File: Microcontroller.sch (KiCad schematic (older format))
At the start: 32 parts, among them J3 USB_B, J4 SWD, J5 DEBUG, Q1 BC817, U3 STM32F401VETx, U4 USBUF02W6, Y1 8MHz

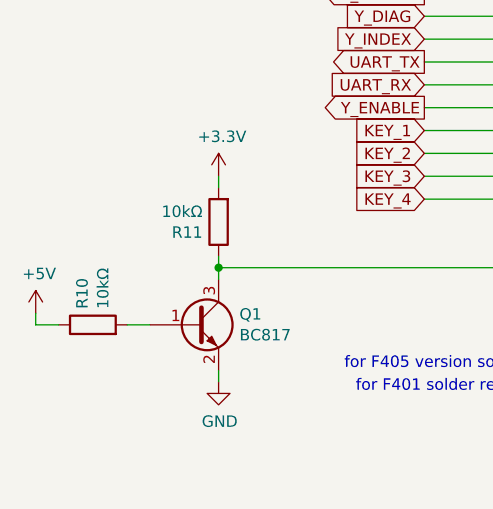
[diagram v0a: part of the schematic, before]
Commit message: Improve Emergency, Added TVS diodes
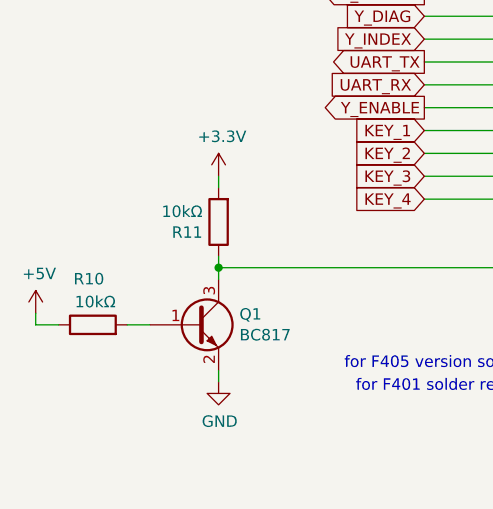
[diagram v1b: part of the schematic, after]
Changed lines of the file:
@@
 AR Path="/5E1018C2/5E3329E9" Ref="R?"  Part="1"
 AR Path="/5DFB2EC0/5E3329E9" Ref="R10"  Part="1"
-F 0 "R10" H 1120 6546 50  0000 L CNN
-F 1 "10kΩ" H 1120 6455 50  0000 L CNN
+F 0 "R10" V 1250 6450 50  0000 L CNN
+F 1 "10kΩ" V 1150 6400 50  0000 L CNN
 F 2 "Resistor_SMD:R_0603_1608Metric" V 980 6500 50  0001 C CNN
 F 3 "~" H 1050 6500 50  0001 C CNN
@@
 Connection ~ 4350 1200
 $Comp
-L power:PWR_FLAG #FLG05
+L power:PWR_FLAG #FLG01
 U 1 1 5E51609C
 P 8850 5750
-F 0 "#FLG05" H 8850 5825 50  0001 C CNN
+F 0 "#FLG01" H 8850 5825 50  0001 C CNN
 F 1 "PWR_FLAG" H 8850 5923 50  0000 C CNN
 F 2 "" H 8850 5750 50  0001 C CNN
@@
 	9900 5200 9900 5250
 $Comp
-L power:PWR_FLAG #FLG06
+L power:PWR_FLAG #FLG02
 U 1 1 5E56BFE7
 P 8950 5250
-F 0 "#FLG06" H 8950 5325 50  0001 C CNN
+F 0 "#FLG02" H 8950 5325 50  0001 C CNN
 F 1 "PWR_FLAG" H 8950 5423 50  0000 C CNN
 F 2 "" H 8950 5250 50  0001 C CNN

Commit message: Update USBUF02W6
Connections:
- net D-: now reaches J3.2 (D-), U4.4 (D3)
- net D+: now reaches J3.3 (D+), U4.6 (D4)
- net USB_DM renamed USB_D-
- net USB_DP renamed USB_D+
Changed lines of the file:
@@
 	4650 3950 5000 3950
 Text GLabel 5000 2750 2    50   BiDi ~ 0
-USB_DP
-Text GLabel 5000 2650 2    50   BiDi ~ 0
-USB_DM
+USB_D+
 Wire Wire Line
 	4650 2650 5000 2650
@@
 	8600 1400 8600 1450
 Text GLabel 9150 1800 2    50   BiDi ~ 0
-USB_DM
+USB_D-
 Text GLabel 9150 1700 2    50   BiDi ~ 0
-USB_DP
+USB_D+
 Wire Wire Line
 	8950 1700 9150 1700
@@
 Wire Wire Line
 	2750 2050 2750 2250
+Text Label 8050 1700 0    50   ~ 0
+D+
+Text Label 8050 1800 0    50   ~ 0
+D-
+Text GLabel 5000 2650 2    50   BiDi ~ 0
+USB_D-
 $EndSCHEMATC

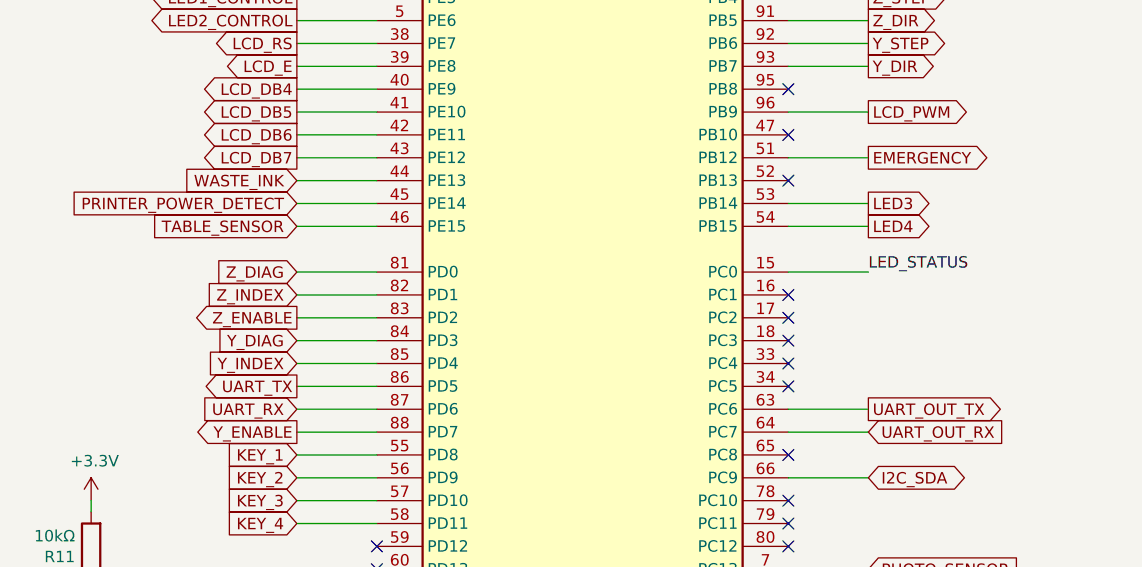
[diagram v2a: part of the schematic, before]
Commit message: Added 12V regulator, aditional input, outputs, improved inputs ESD
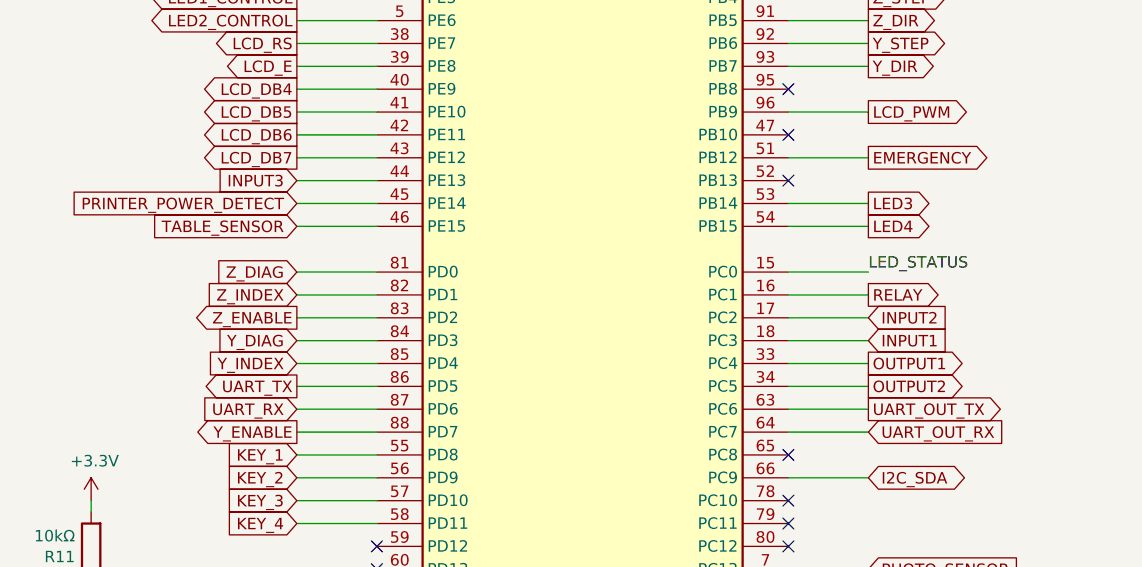
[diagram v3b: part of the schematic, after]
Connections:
- net RELAY: now reaches U3.16 (PC1)
- net INPUT2: now reaches U3.17 (PC2)
- net INPUT1: now reaches U3.18 (PC3)
- net OUTPUT1: now reaches U3.33 (PC4)
- net OUTPUT2: now reaches U3.34 (PC5)
- net WASTE_INK renamed INPUT3
- no-connect marks 28 -> 23
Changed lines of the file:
@@
 Text GLabel 2500 3350 0    50   Input ~ 0
 LIMIT_Y_FRONT
-Text GLabel 2500 4450 0    50   Input ~ 0
-WASTE_INK
 Text GLabel 5000 1750 2    50   Output ~ 0
 PE_SIGNAL
@@
 	5000 4650 4650 4650
 Wire Wire Line
-	2500 4450 2850 4450
-Wire Wire Line
 	4650 6150 5000 6150
 Wire Wire Line
@@
 NoConn ~ 4650 4250
 NoConn ~ 4650 4450
-NoConn ~ 4650 4950
-NoConn ~ 4650 5050
-NoConn ~ 4650 5150
-NoConn ~ 4650 5250
-NoConn ~ 4650 5350
 NoConn ~ 4650 5650
 NoConn ~ 4650 5850
@@
 Text GLabel 5000 2650 2    50   BiDi ~ 0
 USB_D-
+Text GLabel 2500 4450 0    50   Input ~ 0
+INPUT3
+Text GLabel 5000 5250 2    50   Output ~ 0
+OUTPUT1
+Text GLabel 5000 5350 2    50   Output ~ 0
+OUTPUT2
+Text GLabel 5000 5150 2    50   Input ~ 0
+INPUT1
+Text GLabel 5000 5050 2    50   Input ~ 0
+INPUT2
+Wire Wire Line
+	5000 5050 4650 5050
+Wire Wire Line
+	4650 5150 5000 5150
+Wire Wire Line
+	5000 5250 4650 5250
+Wire Wire Line
+	4650 5350 5000 5350
+Wire Wire Line
+	2500 4450 2850 4450
+Text GLabel 5000 4950 2    50   Output ~ 0
+RELAY
+Wire Wire Line
+	4650 4950 5000 4950
 $EndSCHEMATC

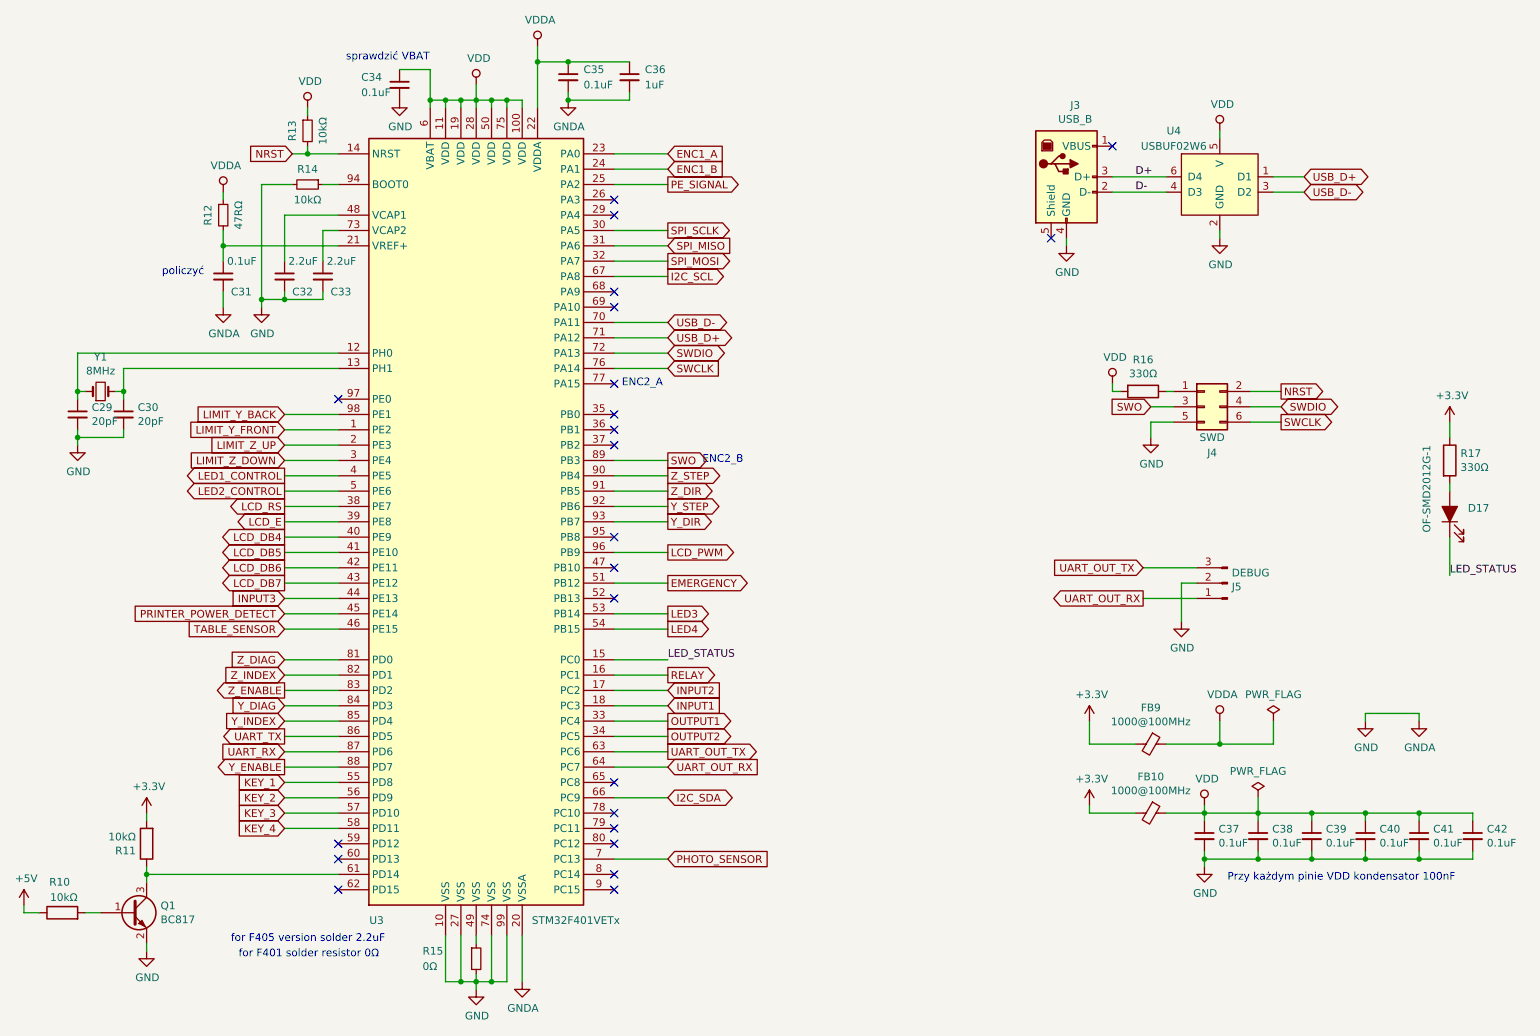
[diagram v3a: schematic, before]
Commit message: Added analog input
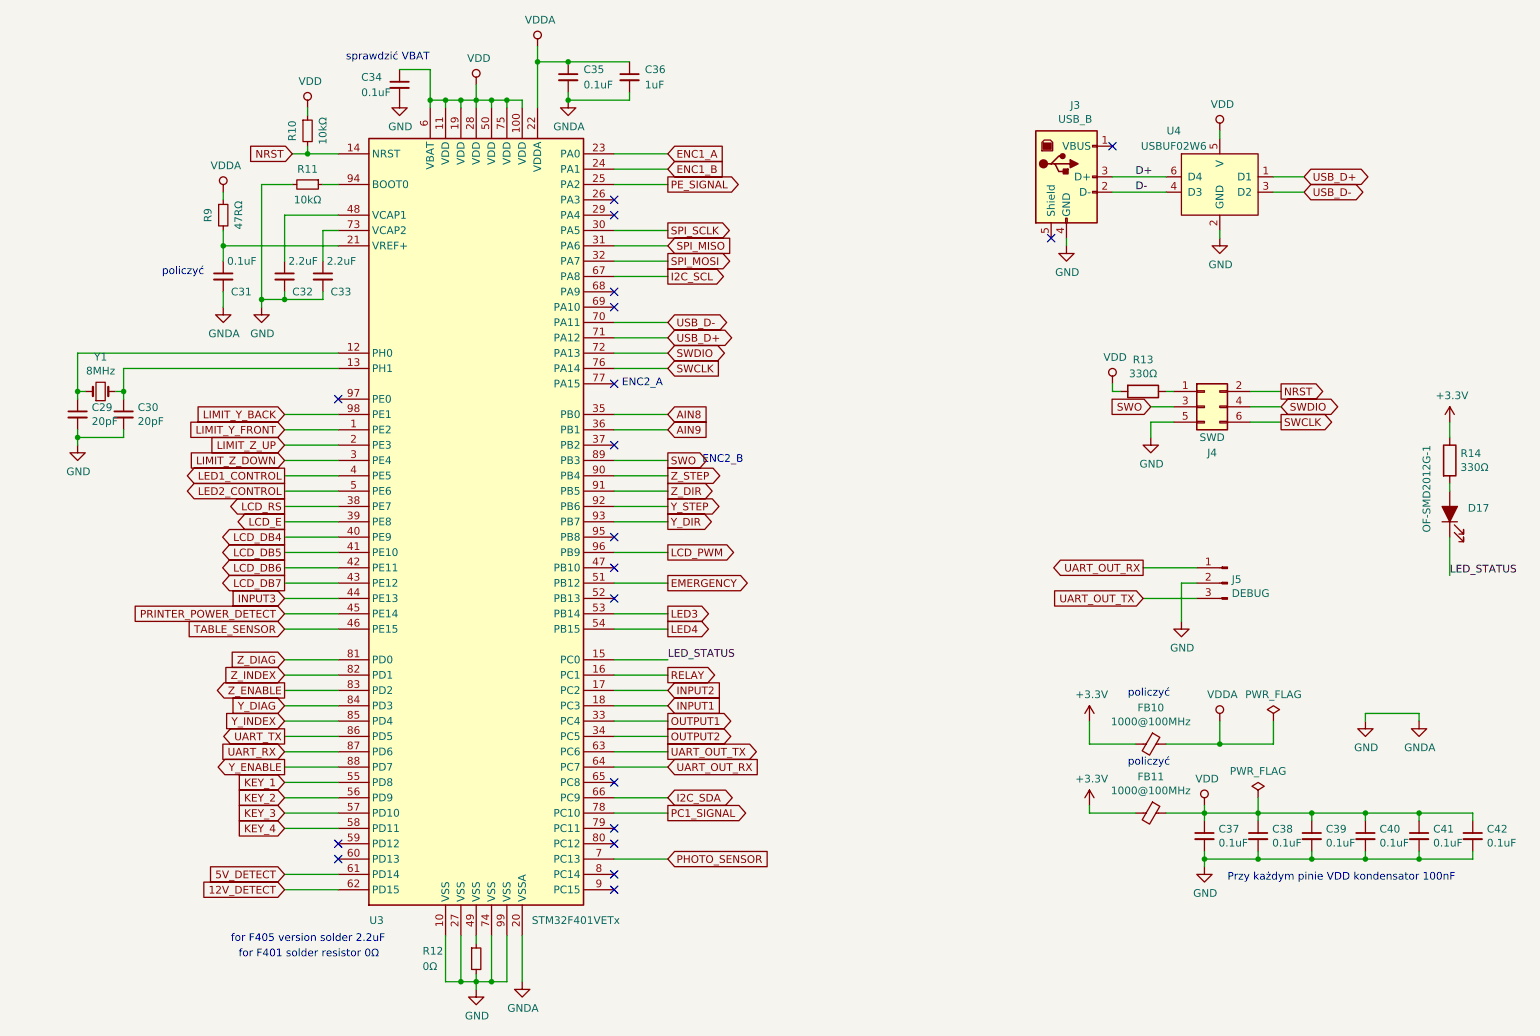
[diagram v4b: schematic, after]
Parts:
- removed Q1: BC817, Package_TO_SOT_SMD:SOT-23, symbol Transistor_BJT:BC817
- removed R10, R11: 10kΩ, Resistor_SMD:R_0603_1608Metric, symbol Device:R
- renumbered FB9 to FB10, FB10 to FB11, R13 to R10, R14 to R11, R15 to R12, R16 to R13, R17 to R14, R12 to R9
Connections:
- net AIN8: now reaches U3.35 (PB0)
- net AIN9: now reaches U3.36 (PB1)
- net 5V_DETECT: now reaches U3.61 (PD14)
- net 12V_DETECT: now reaches U3.62 (PD15)
- net PC1_SIGNAL: now reaches U3.78 (PC10)
- no-connect marks 23 -> 19

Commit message: Improve ESD Protection for TMC2209, Fuses. Schematic ready v1
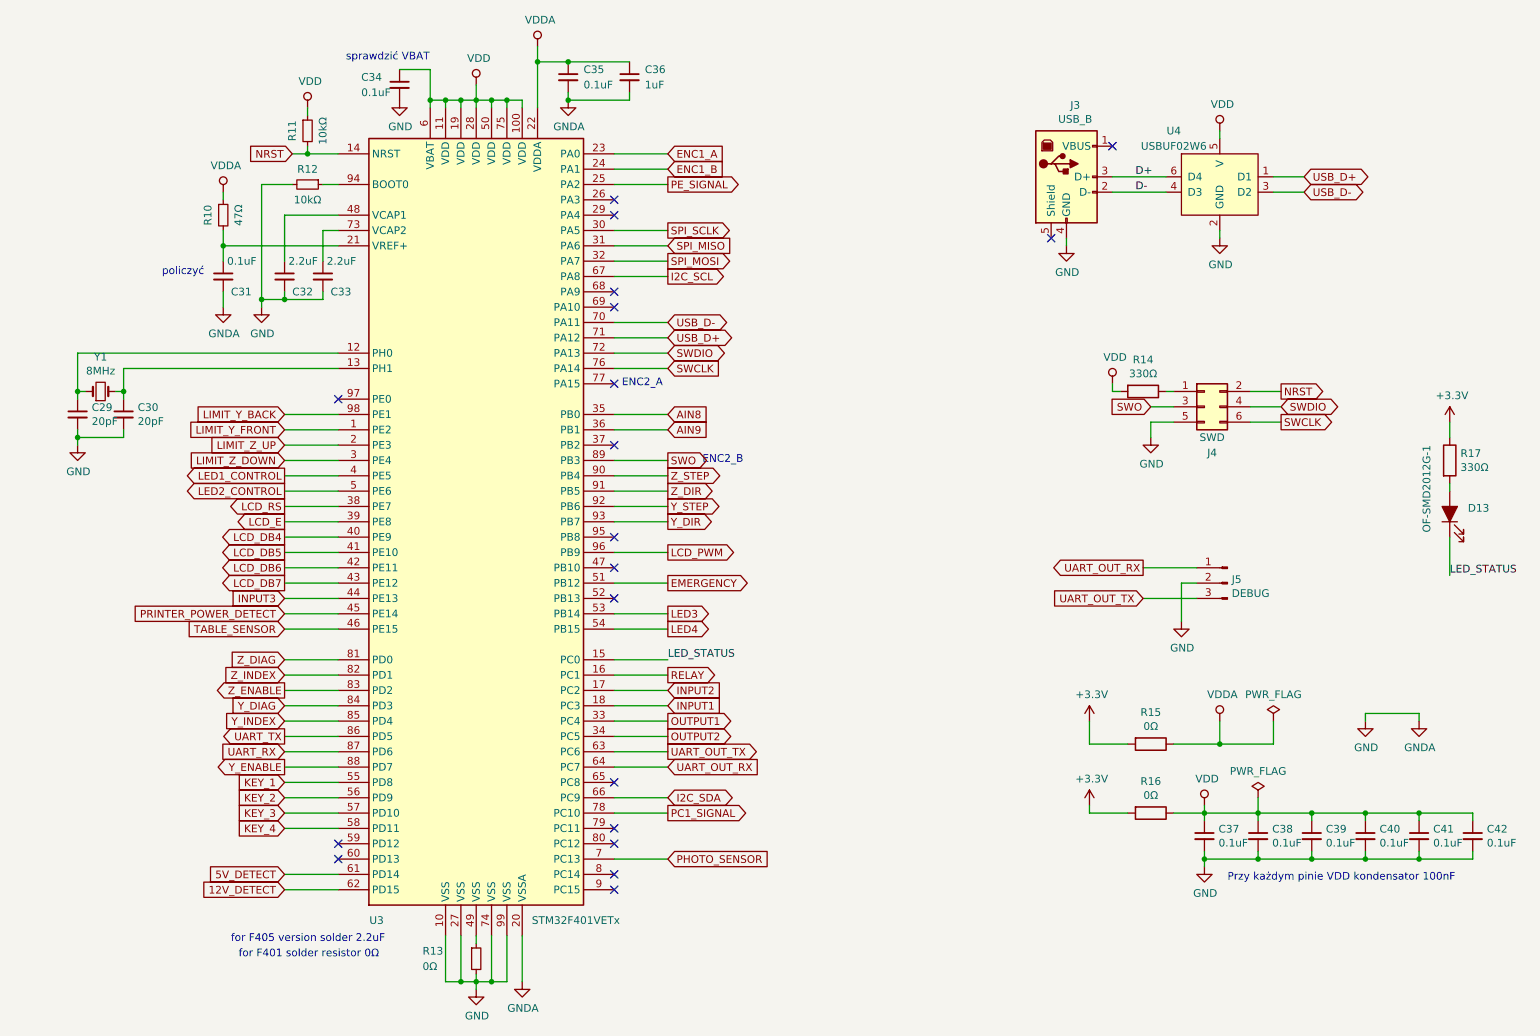
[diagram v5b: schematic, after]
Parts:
- removed FB10, FB11: 1000@100MHz, Inductor_SMD:L_0805_2012Metric, symbol Device:Ferrite_Bead_Small
- added R15, R16: 0Ω, Resistor_SMD:R_0603_1608Metric, symbol Device:R
- R10: renamed from R9; value 47RΩ -> 47Ω
- renumbered D17 to D13, R10 to R11, R11 to R12, R12 to R13, R13 to R14, R14 to R17
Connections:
- net +3V3: now also R15.2, R16.2
- net VDD: now also R16.1
- net VDDA: now also R15.1

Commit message: Update Crystal footprint and inductor 3D package on PCB
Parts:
- Y1: footprint Crystal:Crystal_HC49-U_Vertical -> Crystal:Crystal_HC49-4H_Vertical
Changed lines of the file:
@@
 F 0 "Y1" H 1300 3325 50  0000 C CNN
 F 1 "8MHz" H 1300 3234 50  0000 C CNN
-F 2 "Crystal:Crystal_HC49-U_Vertical" H 1300 3100 50  0001 C CNN
+F 2 "Crystal:Crystal_HC49-4H_Vertical" H 1300 3100 50  0001 C CNN
 F 3 "~" H 1300 3100 50  0001 C CNN
 F 4 "1.6356" H 1300 3100 50  0001 C CNN "Cena"

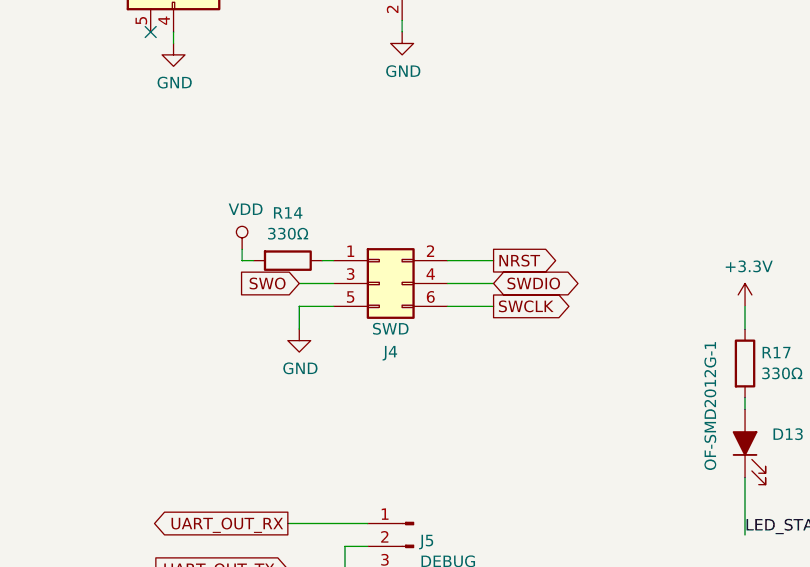
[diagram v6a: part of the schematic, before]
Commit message: Change SWD IDC connector to TC2030
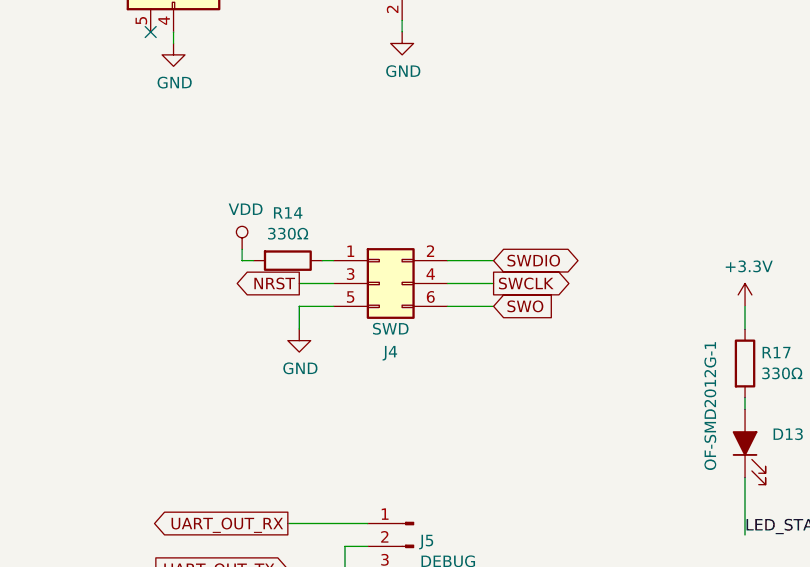
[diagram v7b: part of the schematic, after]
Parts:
- J4: footprint Connector_IDC:IDC-Header_2x03_P2.54mm_Vertical -> Connector:Tag-Connect_TC2030-IDC-NL_2x03_P1.27mm_Vertical; Cena 1.5839 -> (none); Link https://www.tme.eu/pl/details/t821-1-06-s1/zlacza-idc/amphe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 -> (none); Model T821106A1S100CEU -> (none); Opis Gniazdo; IDC; męskie; PIN: 6; proste; THT; złocony; 2,54mm;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 -> (none); Producent AMPHENOL -> (none); Typ THT -> (none)
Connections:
- net NRST: now also J4.3 (Pin_3); no longer J4.2 (Pin_2)
- net SWCLK: now also J4.4 (Pin_4); no longer J4.6 (Pin_6)
- net SWDIO: now also J4.2 (Pin_2); no longer J4.4 (Pin_4)
- net SWO: now also J4.6 (Pin_6); no longer J4.3 (Pin_3)
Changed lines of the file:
@@
 F 0 "J4" H 8550 2900 50  0000 C CNN
 F 1 "SWD" H 8550 3000 50  0000 C CNN
-F 2 "Connector_IDC:IDC-Header_2x03_P2.54mm_Vertical" H 8500 3200 50  0001 C CNN
+F 2 "Connector:Tag-Connect_TC2030-IDC-NL_2x03_P1.27mm_Vertical" H 8500 3200 50  0001 C CNN
 F 3 "~" H 8500 3200 50  0001 C CNN
-F 4 "1.5839" H 8500 3200 50  0001 C CNN "Cena"
-F 5 "https://www.tme.eu/pl/details/t821-1-06-s1/zlacza-idc/amphenol/t821106a1s100ceu/" H 8500 3200 50  0001 C CNN "Link"
-F 6 "T821106A1S100CEU" H 8500 3200 50  0001 C CNN "Model"
-F 7 "Gniazdo; IDC; męskie; PIN: 6; proste; THT; złocony; 2,54mm; Układ: 2x3" H 8500 3200 50  0001 C CNN "Opis"
-F 8 "AMPHENOL" H 8500 3200 50  0001 C CNN "Producent"
-F 9 "THT" H 8500 3200 50  0001 C CNN "Typ"
+F 4 "" H 8500 3200 50  0001 C CNN "Cena"
+F 5 "" H 8500 3200 50  0001 C CNN "Link"
+F 6 "" H 8500 3200 50  0001 C CNN "Model"
+F 7 "" H 8500 3200 50  0001 C CNN "Opis"
+F 8 "" H 8500 3200 50  0001 C CNN "Producent"
+F 9 "" H 8500 3200 50  0001 C CNN "Typ"
 	1    8500 3200
 	1    0    0    -1
@@
 	1    0    0    -1
 $EndComp
-Text GLabel 9000 3100 2    50   Output ~ 0
+Text GLabel 8150 3200 0    50   Output ~ 0
 NRST
-Text GLabel 9000 3200 2    50   BiDi ~ 0
+Text GLabel 9000 3100 2    50   BiDi ~ 0
 SWDIO
 $Comp
@@
 $EndComp
 Wire Wire Line
-	8800 3300 9000 3300
+	8800 3200 9000 3200
 Wire Wire Line
 	8300 3300 8150 3300
@@
 	1    0    0    -1
 $EndComp
-Text GLabel 9000 3300 2    50   Output ~ 0
+Text GLabel 9000 3200 2    50   Output ~ 0
 SWCLK
 Text GLabel 2500 4650 0    50   Input ~ 0
@@
 Wire Wire Line
 	8100 4250 8450 4250
-Text GLabel 8150 3200 0    50   Input ~ 0
+Text GLabel 9000 3300 2    50   Input ~ 0
 SWO
 Wire Wire Line
-	8150 3200 8300 3200
+	9000 3300 8800 3300
+Wire Wire Line
+	8300 3200 8150 3200
 Wire Wire Line
 	8800 3100 9000 3100
-Wire Wire Line
-	8800 3200 9000 3200
 $Comp
 L Device:R R?

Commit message: Change USB Horizontal to Vertical
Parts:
- J3: footprint Connector_USB:USB_B_OST_USB-B1HSxx_Horizontal -> Connector_USB:USB_B_TE_5787834_Vertical
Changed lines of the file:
@@
 F 0 "J3" H 7657 2167 50  0000 C CNN
 F 1 "USB_B" H 7657 2076 50  0000 C CNN
-F 2 "Connector_USB:USB_B_OST_USB-B1HSxx_Horizontal" H 7750 1650 50  0001 C CNN
+F 2 "Connector_USB:USB_B_TE_5787834_Vertical" H 7750 1650 50  0001 C CNN
 F 3 " ~" H 7750 1650 50  0001 C CNN
 F 4 "2.9560" H 7600 1700 50  0001 C CNN "Cena"
